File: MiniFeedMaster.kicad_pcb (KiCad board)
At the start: 2 copper layers, 58.4 x 83.2 mm, 120 parts, among them J1 SWD, J2 CAN, J3 UART, J4 USB, J5 Feeder, J6 Chain, J7 VIn, J8 I2C, J9 EXT, SW1 Button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

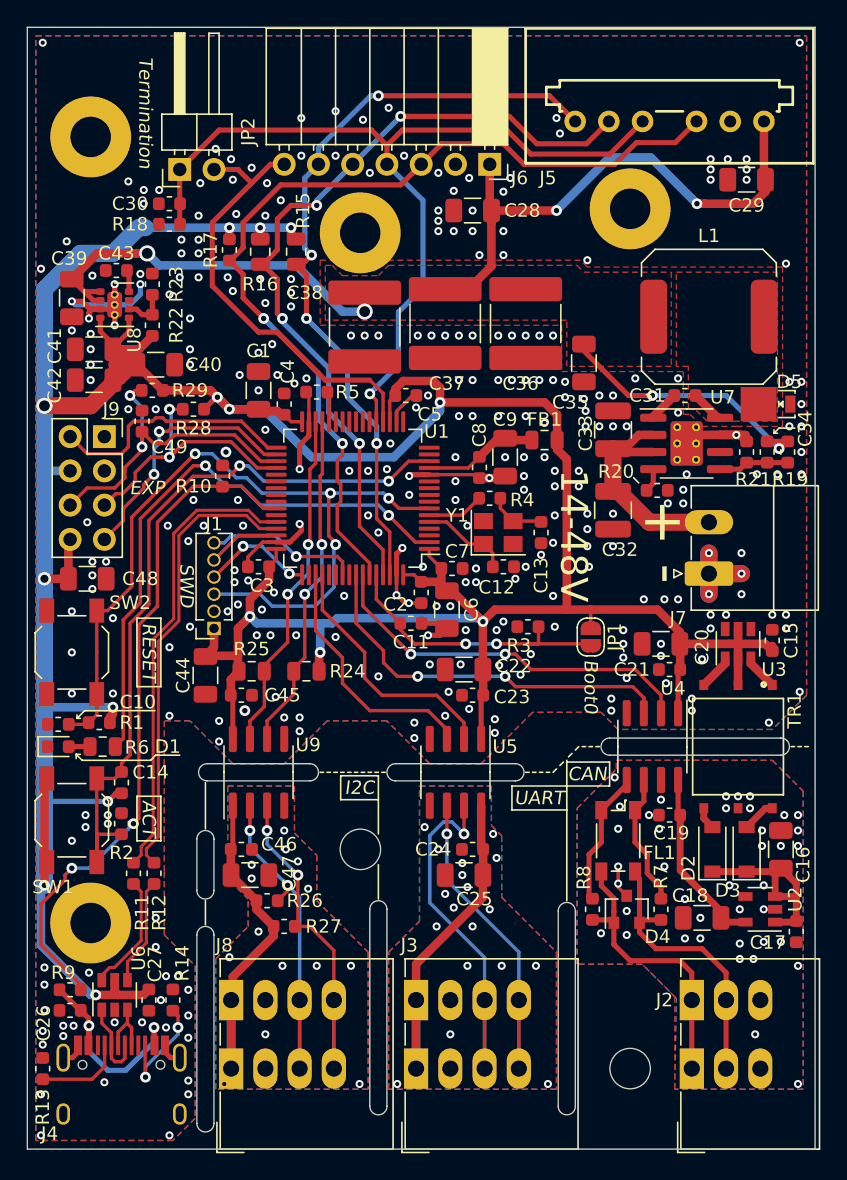
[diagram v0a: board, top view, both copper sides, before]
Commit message: Added IO Protection Switched Fault Signal to +3.3V Added Voltage sensing Added correct UART pins to EXT header
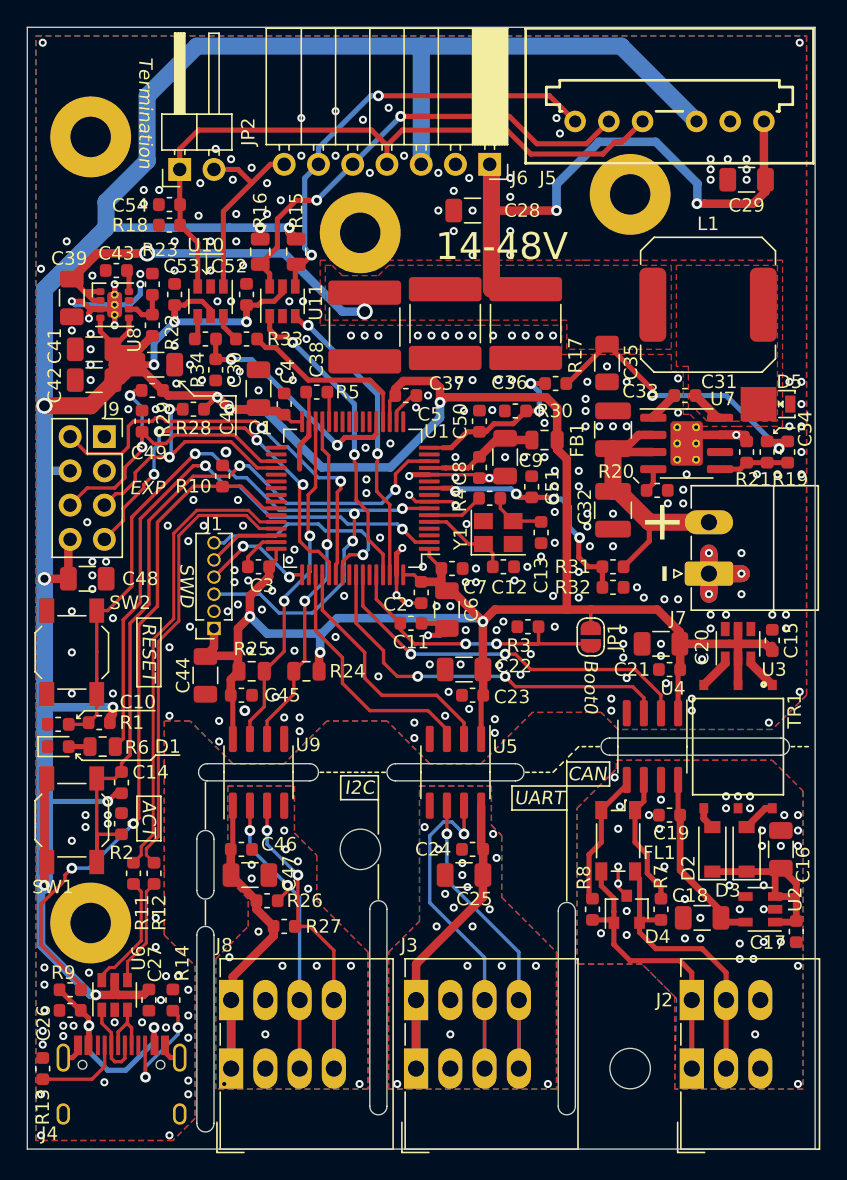
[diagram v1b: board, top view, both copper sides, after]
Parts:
- added C50: 100n, Capacitor_SMD:C_0603_1608Metric, F.Cu at (238.6, 58.4)
- added C51: 100n, Capacitor_SMD:C_0603_1608Metric, F.Cu at (242.5, 63.3)
- added C52: 100n, Capacitor_SMD:C_0603_1608Metric, F.Cu at (221.4, 49.0)
- added C53: 100n, Capacitor_SMD:C_0603_1608Metric, F.Cu at (216.0, 49.0)
- added C54: 100n, Capacitor_SMD:C_0603_1608Metric, F.Cu at (215.6, 42.4)
- added R30: 10k, Resistor_SMD:R_0603_1608Metric, F.Cu at (241.3, 57.7)
- added R31: 150k, Resistor_SMD:R_0603_1608Metric, F.Cu at (248.5, 69.2)
- added R32: 10k, Resistor_SMD:R_0603_1608Metric, F.Cu at (248.5, 70.7)
- added R33: 100R, Resistor_SMD:R_0603_1608Metric, F.Cu at (221.4, 52.3)
- added R34: 10k, Resistor_SMD:R_0603_1608Metric, F.Cu at (218.3, 52.3)
- added U10: USBLC6-2SC6, Package_TO_SOT_SMD:SOT-23-6, F.Cu at (218.7, 49.5)
- added U11: USBLC6-2SC6, Package_TO_SOT_SMD:SOT-23-6, F.Cu at (224.0, 49.5)
- D5: value SS2PH10-M3 -> SS2P4HM3
- R17: value 10k -> 150k
- moved R17 26.1 mm to (244.3, 55.6), turned to 180 degrees
- moved C30 12.8 mm to (219.1, 54.6), turned to 270 degrees
- moved C35 1.71 mm to (248.1, 54.1)
- moved G*** 1.52 mm to (248.0, 51.1)
- moved G*** 1.52 mm to (257.6, 51.1)
- moved REF** 1.07 mm to (249.8, 41.6)
- moved L1 0.89 mm to (255.6, 49.8)
- moved REF** 0.63 mm to (238.4, 50.4)
- moved C1 0.13 mm to (222.2, 56.0)
- moved R18 0.06 mm to (215.6, 43.9)
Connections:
- J5 pad 3: /FD_FAULT -> +3V3
- J5 pad 4: /FD_FB -> Net-(C54-Pad1)
- J5 pad 5: /FD_SCL -> /FeederInterface/OUT_SCL
- J5 pad 6: /FD_SDA -> /FeederInterface/OUT_SDA
- J6 pad 3: /FD_FAULT -> +3V3
- J6 pad 4: /FD_FB -> Net-(C54-Pad1)
- J6 pad 5: /FD_SCL -> /FeederInterface/OUT_SCL
- J6 pad 6: /FD_SDA -> /FeederInterface/OUT_SDA
- J6 pad 7: /FD_ID -> /FeederInterface/V_ID_RAW
- JP2 pad 1: /FD_FB -> Net-(C54-Pad1)
- JP2 pad 2: /FD_ID -> /FeederInterface/V_ID_RAW
- R15 pad 2: /FD_SDA -> /FeederInterface/OUT_SDA
- R16 pad 2: /FD_SCL -> /FeederInterface/OUT_SCL
- R17 pad 1: +3V3 -> +12V
- R17 pad 2: /FD_FAULT -> Net-(C50-Pad1)
- R18 pad 1: /FD_FB -> Net-(C54-Pad1)
- U1 pad 10: (no net) -> Net-(C51-Pad1)
- U1 pad 16: (no net) -> Net-(C50-Pad1)
- U1 pad 33: /EXT_RX -> (no net)
- U1 pad 34: /EXT_TX -> (no net)
- U1 pad 53: (no net) -> /EXT_TX
- U1 pad 54: (no net) -> /EXT_RX
- U1 pad 59: /FD_FAULT -> (no net)
- U1 pad 8: (no net) -> GND
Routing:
- net +3V3: track 301.2 -> 385.8 mm, vias 15 -> 17
- net /FD_FAULT: track 69.4 -> 0.00 mm, vias 2 -> 0
- net Net-(C54-Pad1): track 0.00 -> 49.7 mm
- net /FD_FB: track 65.7 -> 17.3 mm, vias 1 -> 2
- net /FD_SCL: track 60.4 -> 23.1 mm, vias 4 -> 2
- net /FeederInterface/OUT_SCL: track 0.00 -> 35.3 mm, vias 0 -> 2
- net /FD_SDA: track 57.3 -> 22.3 mm, vias 4 -> 2
- net /FeederInterface/OUT_SDA: track 0.00 -> 33.1 mm, vias 0 -> 2
- net /FD_ID: track 33.1 -> 13.1 mm
- net Net-(C51-Pad1): track 0.00 -> 18.8 mm, vias 0 -> 4
- net /FeederInterface/V_ID_RAW: track 0.00 -> 14.7 mm
- net /EXT_RX: track 18.7 -> 31.6 mm, vias 0 -> 2
- net Net-(C50-Pad1): track 0.00 -> 12.6 mm, vias 0 -> 2
- net /EXT_TX: track 19.3 -> 30.3 mm, vias 2 -> 4
- net +12V: track 91.1 -> 99.5 mm
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
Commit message: Added LEDs to indicate power on the 12V and 3.3V rails Added Fiducials Moved references for SW1 and R2 Added 3D Model
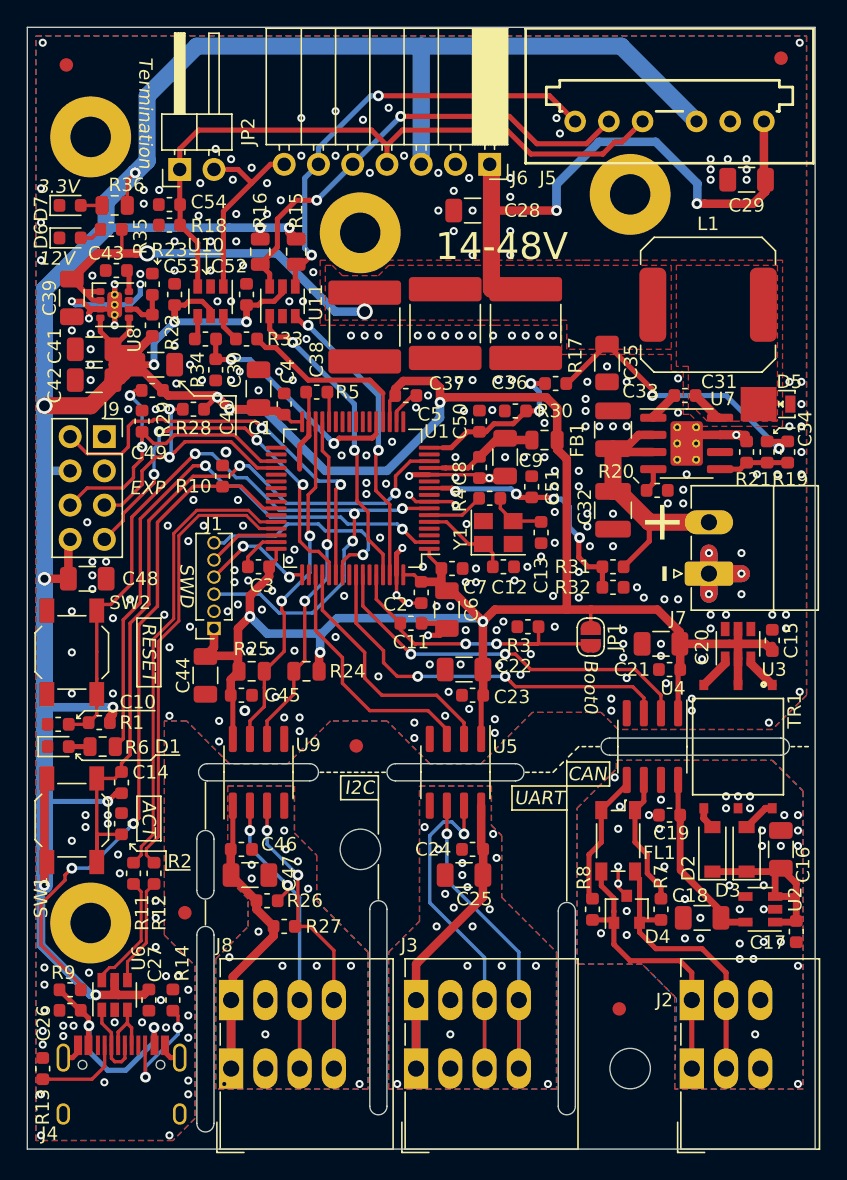
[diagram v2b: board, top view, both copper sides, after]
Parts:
- added D6: RED, LED_SMD:LED_0603_1608Metric, F.Cu at (208.3, 44.8)
- added D7: RED, LED_SMD:LED_0603_1608Metric, F.Cu at (208.3, 42.4)
- added Fid1: Fiducial_1mm_Mask2mm, Fiducial:Fiducial_1mm_Mask2mm, F.Cu at (208.0, 32.0)
- added Fid2: Fiducial_1mm_Mask2mm, Fiducial:Fiducial_1mm_Mask2mm, F.Cu at (249.0, 102.0)
- added Fid3: Fiducial_1mm_Mask2mm, Fiducial:Fiducial_1mm_Mask2mm, F.Cu at (261.0, 31.5)
- added Fid4: Fiducial_1mm_Mask2mm, Fiducial:Fiducial_1mm_Mask2mm, F.Cu at (229.5, 82.5)
- added Fid5: Fiducial_1mm_Mask2mm, Fiducial:Fiducial_1mm_Mask2mm, F.Cu at (216.8, 94.9)
- added R35: 10k, Resistor_SMD:R_0603_1608Metric, F.Cu at (211.3, 44.2)
- added R36: 1k5, Resistor_SMD:R_0805_2012Metric, F.Cu at (211.6, 42.4)
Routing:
- net +3V3: track 385.8 -> 388.4 mm, vias 17 -> 18
- net +12V: track 99.5 -> 101.3 mm
- net Net-(D6-Pad2): track 0.00 -> 1.74 mm
- net Net-(D7-Pad2): track 0.00 -> 1.58 mm
- net GND: vias 286 -> 295
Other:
- board text added: "12V"
- board text added: "3.3V"
- board text added: "v1.0"
